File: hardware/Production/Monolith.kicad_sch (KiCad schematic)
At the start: 0 parts

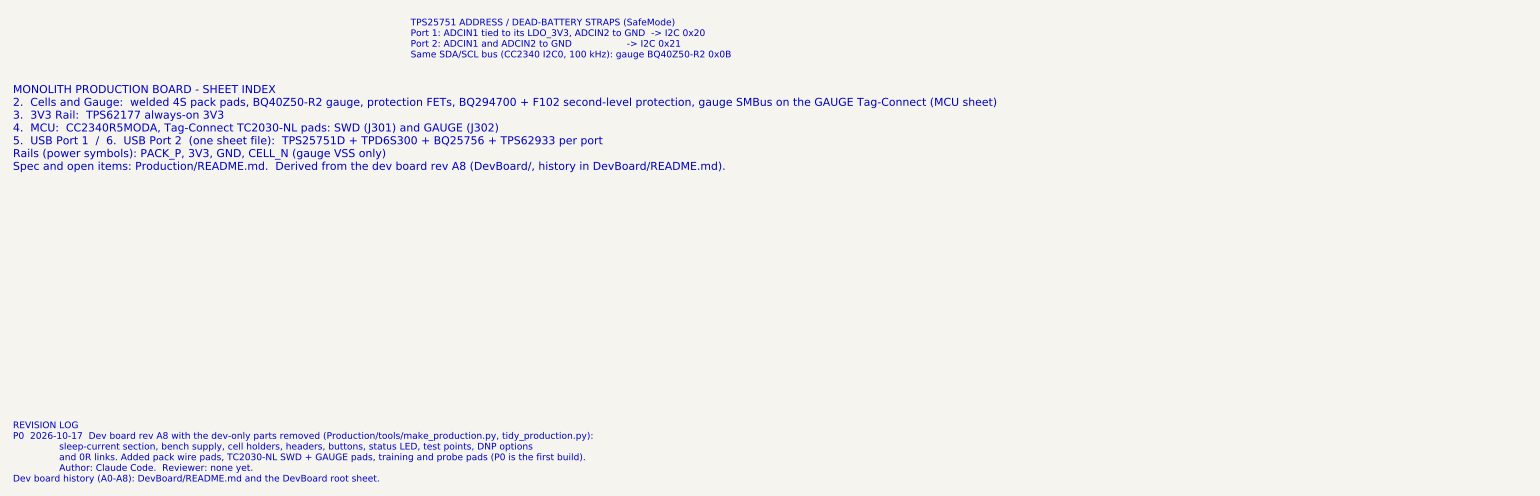
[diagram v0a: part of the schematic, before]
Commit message: Production board: tail slots, 1N/4P Kelvin nets, carrier peg holes, cup keep-outs
Schematic (make_production.py, regenerated):
- J108-J112 become plated slots for the nickel tails; J115 (1N) and J116 (4P)
  are the Kelvin fingers on new nets CELL_1N / CELL_4P (SLUA660 2.3-2.4).
  CELL_1N: gauge VSS star, U102 VSS, decoupling, NTC returns. CELL_4P: VC4,
  U102 V4/VDD, D101. Shunt, SRP and Q104 stay on CELL_N; F102 on CELL_P_RAW.
- H101-H104: cover standoffs -> 2.2 mm NPTH carrier peg holes.
- R413/R513 11.8k and the ICHG heading now come from the generator.
- Symbol uuids are kept across regens so Update PCB keeps placed parts.
- check_netlist accepts "new NAME" net moves; tidy notes updated.

Board: cup keep-outs (rails split at the filler, gap filler, tail runs,
vent, antenna, top stops), footprints swapped and nets applied from the
schematic (checked pad by pad), slots and pegs placed and locked.

make_board.py: --keepouts writes zones as text (KiCad 10 python can't build
outlines), --mech replaces --standoffs and keeps the .kicad_pro.
monolith_shell.py holds the cup's board-facing values (CUP_*, cup_rails).
Docs: README sections, p0-assembly solder order and Kelvin wording.

Co-Authored-By: Claude Opus 5.5 <noreply@anthropic.com>
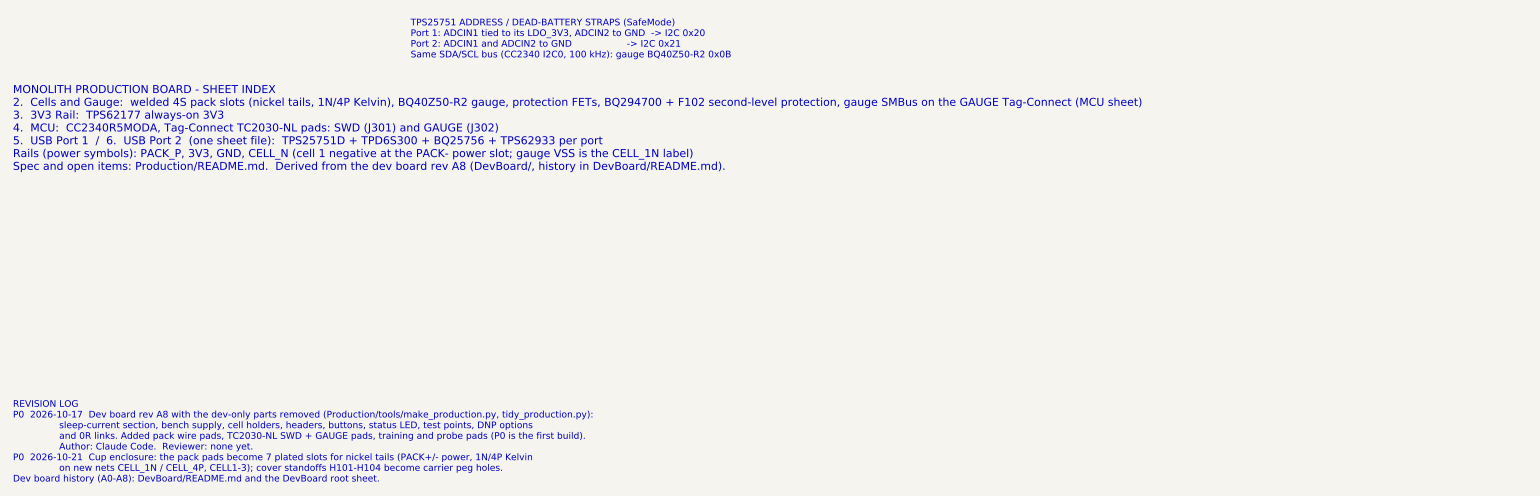
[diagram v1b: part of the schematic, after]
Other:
- note added: "MONOLITH PRODUCTION BOARD - SHEET INDEX 2. Cells and Gauge: welded 4S pack slots (nickel tails, 1N/4P Kelvin), BQ40Z50-R2 gauge, protection FETs, BQ294700 + F102 second-level protection, gauge SMBus on the GAUGE Tag-Connect (MCU sheet) 3. 3V3 Rail: TPS62177 always-on 3V3 4. MCU: CC2340R5MODA, Tag-Connect TC2030-NL pads: SWD (J301) and GAUGE (J302) 5. USB Port 1 / 6. USB Port 2 (one sheet file): T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"
- note added: "REVISION LOG P0 2026-10-17 Dev board rev A8 with the dev-only parts removed (Production/tools/make_production.py, tidy_production.py): sleep-current section, bench supply, cell holders, headers, buttons, status LED, test points, DNP options and 0R links. Added pack wire pads, TC2030-NL SWD + GAUGE pads, training and probe pads (P0 is the first build). Author: Claude Code. Reviewer: none yet. P0 2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"
- note removed: "MONOLITH PRODUCTION BOARD - SHEET INDEX 2. Cells and Gauge: welded 4S pack pads, BQ40Z50-R2 gauge, protection FETs, BQ294700 + F102 second-level protection, gauge SMBus on the GAUGE Tag-Connect (MCU sheet) 3. 3V3 Rail: TPS62177 always-on 3V3 4. MCU: CC2340R5MODA, Tag-Connect TC2030-NL pads: SWD (J301) and GAUGE (J302) 5. USB Port 1 / 6. USB Port 2 (one sheet file): TPS25751D + TPD6S300 + BQ25756 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"
- note removed: "REVISION LOG P0 2026-10-17 Dev board rev A8 with the dev-only parts removed (Production/tools/make_production.py, tidy_production.py): sleep-current section, bench supply, cell holders, headers, buttons, status LED, test points, DNP options and 0R links. Added pack wire pads, TC2030-NL SWD + GAUGE pads, training and probe pads (P0 is the first build). Author: Claude Code. Reviewer: none yet. Dev 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"
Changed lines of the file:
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@@
 		(comment 3 "P0: dev board rev A8 stripped by Production/tools/make_production.py; not reviewed")
 	)
-	(text "MONOLITH PRODUCTION BOARD - SHEET INDEX\n2.  Cells and Gauge:  welded 4S pack pads, BQ40Z50-R2 gauge, protection FETs, BQ294700 + F102 second-level protection, gauge SMBus on the GAUGE Tag-Connect (MCU sheet)\n3.  3V3 Rail:  TPS62177 always-on 3V3\n4.  MCU:  CC2340R5MODA, Tag-Connect TC2030-NL pads: SWD (J301) and GAUGE (J302)\n5.  USB Port 1  /  6.  USB Port 2  (one sheet file):  TPS25751D + TPD6S300 + BQ25756 + TPS62933 per port\nRails (power symbols): PACK_P, 3V3, GND, CELL_N (gauge VSS only)\nSpec and open items: Production/README.md.  Derived from the dev board rev A8 (DevBoard/, history in DevBoard/README.md)."
+	(text "MONOLITH PRODUCTION BOARD - SHEET INDEX\n2.  Cells and Gauge:  welded 4S pack slots (nickel tails, 1N/4P Kelvin), BQ40Z50-R2 gauge, protection FETs, BQ294700 + F102 second-level protection, gauge SMBus on the GAUGE Tag-Connect (MCU sheet)\n3.  3V3 Rail:  TPS62177 always-on 3V3\n4.  MCU:  CC2340R5MODA, Tag-Connect TC2030-NL pads: SWD (J301) and GAUGE (J302)\n5.  USB Port 1  /  6.  USB Port 2  (one sheet file):  TPS25751D + TPD6S300 + BQ25756 + TPS62933 per port\nRails (power symbols): PACK_P, 3V3, GND, CELL_N (cell 1 negative at the PACK- power slot; gauge VSS is the CELL_1N label)\nSpec and open items: Production/README.md.  Derived from the dev board rev A8 (DevBoard/, history in DevBoard/README.md)."
 		(exclude_from_sim no)
 		(at 30.48 205.74 0)
@@
 		)
 	)
-	(text "REVISION LOG\nP0  2026-10-17  Dev board rev A8 with the dev-only parts removed (Production/tools/make_production.py, tidy_production.py):\n                sleep-current section, bench supply, cell holders, headers, buttons, status LED, test points, DNP options\n                and 0R links. Added pack wire pads, TC2030-NL SWD + GAUGE pads, training and probe pads (P0 is the first build).\n                Author: Claude Code.  Reviewer: none yet.\nDev board history (A0-A8): DevBoard/README.md and the DevBoard root sheet."
+	(text "REVISION LOG\nP0  2026-10-17  Dev board rev A8 with the dev-only parts removed (Production/tools/make_production.py, tidy_production.py):\n                sleep-current section, bench supply, cell holders, headers, buttons, status LED, test points, DNP options\n                and 0R links. Added pack wire pads, TC2030-NL SWD + GAUGE pads, training and probe pads (P0 is the first build).\n                Author: Claude Code.  Reviewer: none yet.\nP0  2026-10-21  Cup enclosure: the pack pads become 7 plated slots for nickel tails (PACK+/- power, 1N/4P Kelvin\n                on new nets CELL_1N / CELL_4P, CELL1-3); cover standoffs H101-H104 become carrier peg holes.\nDev board history (A0-A8): DevBoard/README.md and the DevBoard root sheet."
 		(exclude_from_sim no)
 		(at 30.48 265.43 0)

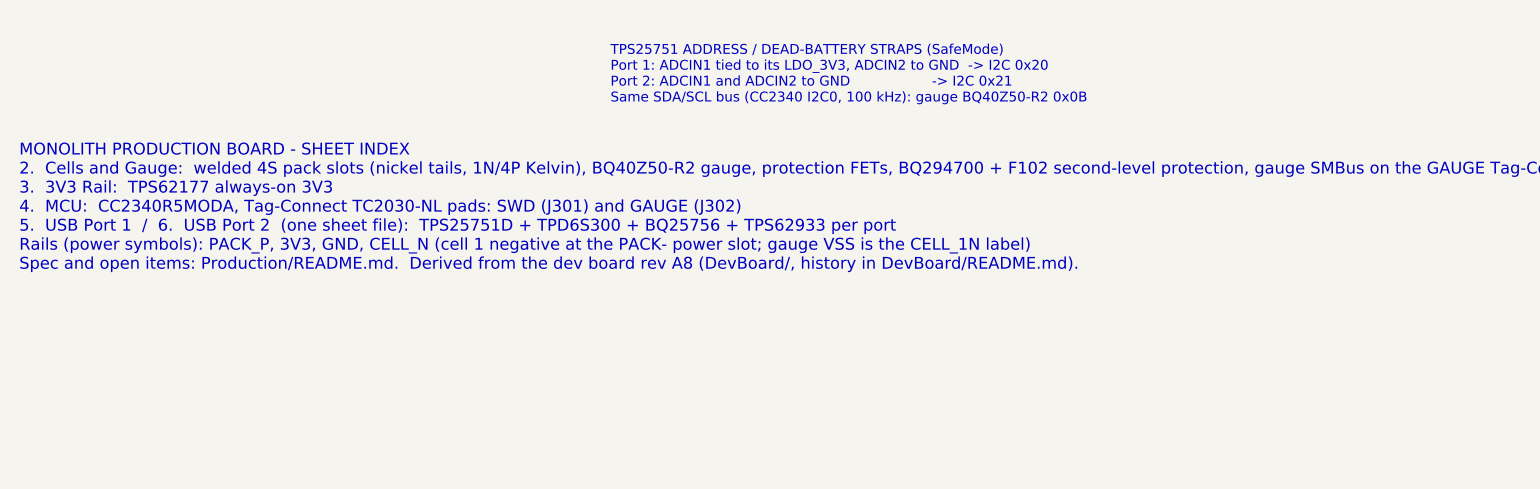
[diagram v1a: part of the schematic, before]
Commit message: Production board: PACK wire holes for the option C wire tails
J108 / J112 go from the 4.6 mm PACK power slots to Ø1.5 mm plated holes
(0.4 mm ring) for the 18 AWG thin-wall PTFE power wires, at sb_pack_holes():
KiCad (86.975, 135.7255) and (113.025, 135.7255), F.Cu, locked. The Kelvin
wires stay in the J115 / J116 slots.

- make_production.py: WIRE_FP footprint generated from SB_PWIRE_*, used for
  J108 / J112; SLOT_REFS keeps the five slots, WIRE_REFS the two holes.
- make_board.py: --mech also places the wire holes; keepout_list() follows
  the merged model (three tail runs, four KO_B_wire_* from sb_wire_runs()).
- Board: J108 / J112 swapped and placed as Update PCB + --mech would; the four
  PACK / Kelvin finger tail keep-outs replaced by KO_B_wire_*. Other
  keep-outs untouched (KO_F_above_antenna stays removed).
- Schematic Footprint / Value fields and sheet notes; Slot_Tab_4.6x0.6mm
  dropped from the library; README, spec and assembly docs.

KiCad is not available in this environment, so DRC has not been run; a
script check covers the outline, edge rule, ring and courtyards.

Co-Authored-By: Claude Opus 5.5 (1M context) <noreply@anthropic.com>
Claude-Session: https://claude.ai/code/session_01VT5ZsG8mLjRjzAJFn7LJRo
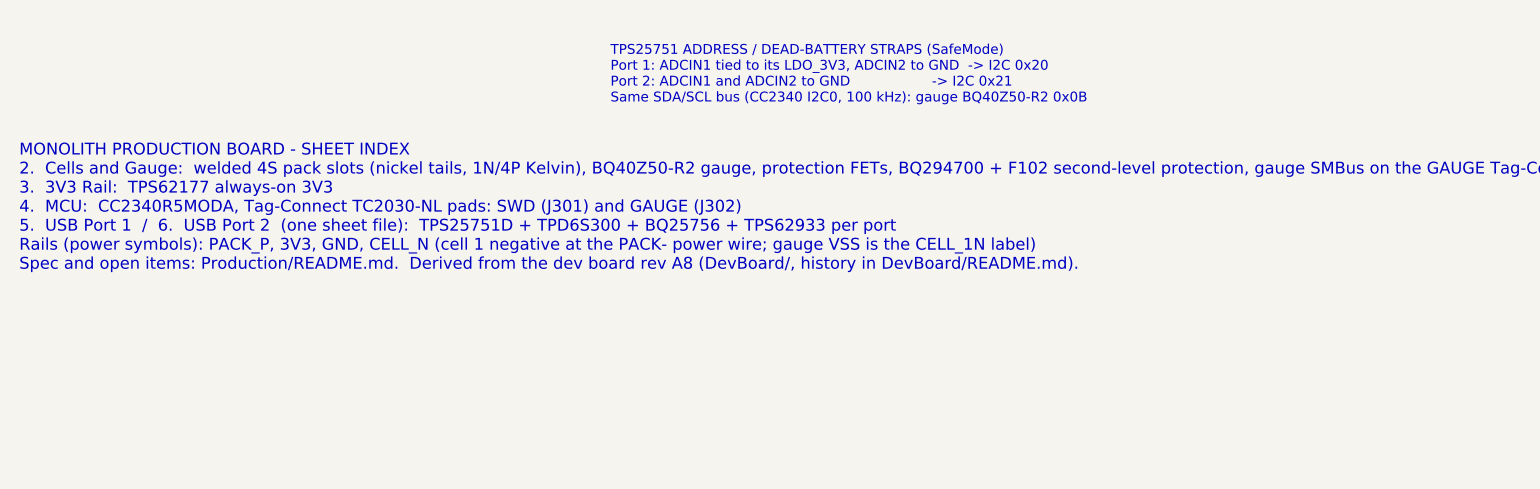
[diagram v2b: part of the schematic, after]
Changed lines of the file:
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@@
 		(comment 3 "P0: dev board rev A8 stripped by Production/tools/make_production.py; not reviewed")
 	)
-	(text "MONOLITH PRODUCTION BOARD - SHEET INDEX\n2.  Cells and Gauge:  welded 4S pack slots (nickel tails, 1N/4P Kelvin), BQ40Z50-R2 gauge, protection FETs, BQ294700 + F102 second-level protection, gauge SMBus on the GAUGE Tag-Connect (MCU sheet)\n3.  3V3 Rail:  TPS62177 always-on 3V3\n4.  MCU:  CC2340R5MODA, Tag-Connect TC2030-NL pads: SWD (J301) and GAUGE (J302)\n5.  USB Port 1  /  6.  USB Port 2  (one sheet file):  TPS25751D + TPD6S300 + BQ25756 + TPS62933 per port\nRails (power symbols): PACK_P, 3V3, GND, CELL_N (cell 1 negative at the PACK- power slot; gauge VSS is the CELL_1N label)\nSpec and open items: Production/README.md.  Derived from the dev board rev A8 (DevBoard/, history in DevBoard/README.md)."
+	(text "MONOLITH PRODUCTION BOARD - SHEET INDEX\n2.  Cells and Gauge:  welded 4S pack slots (nickel tails, 1N/4P Kelvin), BQ40Z50-R2 gauge, protection FETs, BQ294700 + F102 second-level protection, gauge SMBus on the GAUGE Tag-Connect (MCU sheet)\n3.  3V3 Rail:  TPS62177 always-on 3V3\n4.  MCU:  CC2340R5MODA, Tag-Connect TC2030-NL pads: SWD (J301) and GAUGE (J302)\n5.  USB Port 1  /  6.  USB Port 2  (one sheet file):  TPS25751D + TPD6S300 + BQ25756 + TPS62933 per port\nRails (power symbols): PACK_P, 3V3, GND, CELL_N (cell 1 negative at the PACK- power wire; gauge VSS is the CELL_1N label)\nSpec and open items: Production/README.md.  Derived from the dev board rev A8 (DevBoard/, history in DevBoard/README.md)."
 		(exclude_from_sim no)
 		(at 30.48 205.74 0)

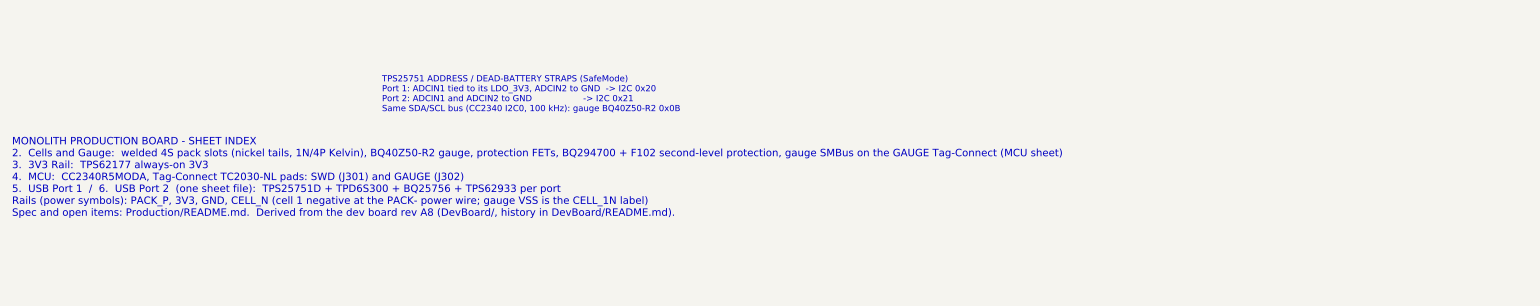
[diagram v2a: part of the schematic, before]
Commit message: Sense leads as wires; cup, cap and carrier fixes from the 2026-10-24 review
Sense wires (Logan): CELL1-3 become 28 AWG PTFE wires like the 1N / 4P
Kelvin leads. CELL1 / CELL3 solder to a short tongue of the top strip just
past the top frame; CELL2 solders to the middle of the bottom strip and runs
in a channel in the bottom frame. The five board pads keep their copper and
get a round 0.8 mm drill instead of the oval slot (J109-J111, J115, J116).

Review fixes in monolith_cup.py:
- cap: outer collar with crush ribs holds the mouth against the O-ring;
  O-ring and screws moved up so each screw has a 1.2 mm ligament; blind
  pilots (no path round the seal); skirt 2.6 mm (1.2 mm root), its top
  1.1 mm under the frame; four overtravel posts; pad printed 1.2 proud and
  relieved under the PACK pads
- carrier: board rails are four clip-on blocks keyed into the frames, so
  the front cells can be loaded; one merged wire notch per side (no loose
  chip); foam preload pockets; CELL2 channel
- peg posts run on to 0.3 mm under a 2.0 mm board-face wall; TPU sleeves
  hold the board on them
- fish-paper insulator rings on the four + ends
- top wall 1.85 mm; USB-C bores sized to the rev A4 ring with 0.15 mm
  squeeze and a lead-in
- new checks: one-piece parts, ligament, blind pilots, skirt gap, preload,
  wall deflection, key slots, channel

Board: R124 / R126 DNP (gauge note 16), so Q104 can't fire F102 while the
pack is wired up.

Co-Authored-By: Claude Opus 5.5 (1M context) <noreply@anthropic.com>
Claude-Session: https://claude.ai/code/session_01V2XuchjL8SPbkwDuzZLoSy
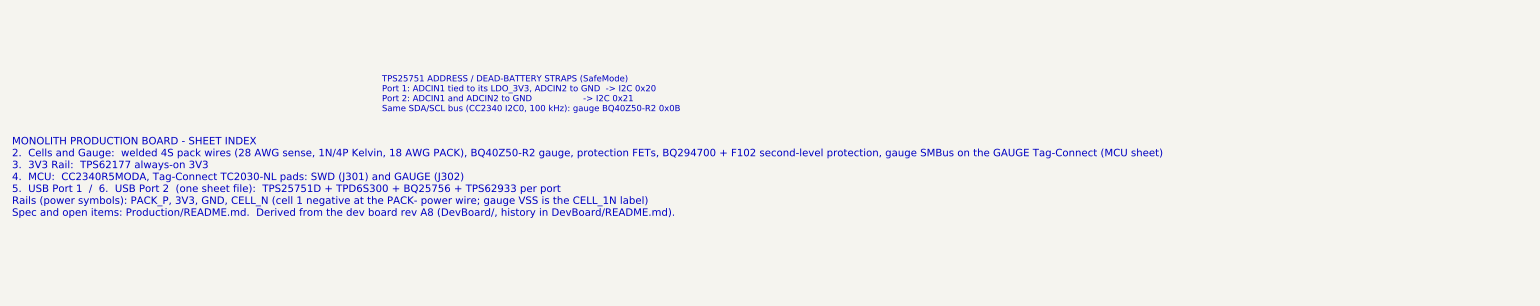
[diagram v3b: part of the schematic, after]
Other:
- note added: "MONOLITH PRODUCTION BOARD - SHEET INDEX 2. Cells and Gauge: welded 4S pack wires (28 AWG sense, 1N/4P Kelvin, 18 AWG PACK), BQ40Z50-R2 gauge, protection FETs, BQ294700 + F102 second-level protection, gauge SMBus on the GAUGE Tag-Connect (MCU sheet) 3. 3V3 Rail: TPS62177 always-on 3V3 4. MCU: CC2340R5MODA, Tag-Connect TC2030-NL pads: SWD (J301) and GAUGE (J302) 5. USB Port 1 / 6. USB Port 2 (one s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"
- note removed: "MONOLITH PRODUCTION BOARD - SHEET INDEX 2. Cells and Gauge: welded 4S pack slots (nickel tails, 1N/4P Kelvin), BQ40Z50-R2 gauge, protection FETs, BQ294700 + F102 second-level protection, gauge SMBus on the GAUGE Tag-Connect (MCU sheet) 3. 3V3 Rail: TPS62177 always-on 3V3 4. MCU: CC2340R5MODA, Tag-Connect TC2030-NL pads: SWD (J301) and GAUGE (J302) 5. USB Port 1 / 6. USB Port 2 (one sheet file): T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"
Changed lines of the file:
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@@
 		(comment 3 "P0: dev board rev A8 stripped by Production/tools/make_production.py; not reviewed")
 	)
-	(text "MONOLITH PRODUCTION BOARD - SHEET INDEX\n2.  Cells and Gauge:  welded 4S pack slots (nickel tails, 1N/4P Kelvin), BQ40Z50-R2 gauge, protection FETs, BQ294700 + F102 second-level protection, gauge SMBus on the GAUGE Tag-Connect (MCU sheet)\n3.  3V3 Rail:  TPS62177 always-on 3V3\n4.  MCU:  CC2340R5MODA, Tag-Connect TC2030-NL pads: SWD (J301) and GAUGE (J302)\n5.  USB Port 1  /  6.  USB Port 2  (one sheet file):  TPS25751D + TPD6S300 + BQ25756 + TPS62933 per port\nRails (power symbols): PACK_P, 3V3, GND, CELL_N (cell 1 negative at the PACK- power wire; gauge VSS is the CELL_1N label)\nSpec and open items: Production/README.md.  Derived from the dev board rev A8 (DevBoard/, history in DevBoard/README.md)."
+	(text "MONOLITH PRODUCTION BOARD - SHEET INDEX\n2.  Cells and Gauge:  welded 4S pack wires (28 AWG sense, 1N/4P Kelvin, 18 AWG PACK), BQ40Z50-R2 gauge, protection FETs, BQ294700 + F102 second-level protection, gauge SMBus on the GAUGE Tag-Connect (MCU sheet)\n3.  3V3 Rail:  TPS62177 always-on 3V3\n4.  MCU:  CC2340R5MODA, Tag-Connect TC2030-NL pads: SWD (J301) and GAUGE (J302)\n5.  USB Port 1  /  6.  USB Port 2  (one sheet file):  TPS25751D + TPD6S300 + BQ25756 + TPS62933 per port\nRails (power symbols): PACK_P, 3V3, GND, CELL_N (cell 1 negative at the PACK- power wire; gauge VSS is the CELL_1N label)\nSpec and open items: Production/README.md.  Derived from the dev board rev A8 (DevBoard/, history in DevBoard/README.md)."
 		(exclude_from_sim no)
 		(at 30.48 205.74 0)
